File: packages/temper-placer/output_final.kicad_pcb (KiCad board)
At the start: 4 copper layers, 100 x 150 mm, 33 parts, among them Q1 IKW40N120H3, Q2 IKW40N120H3

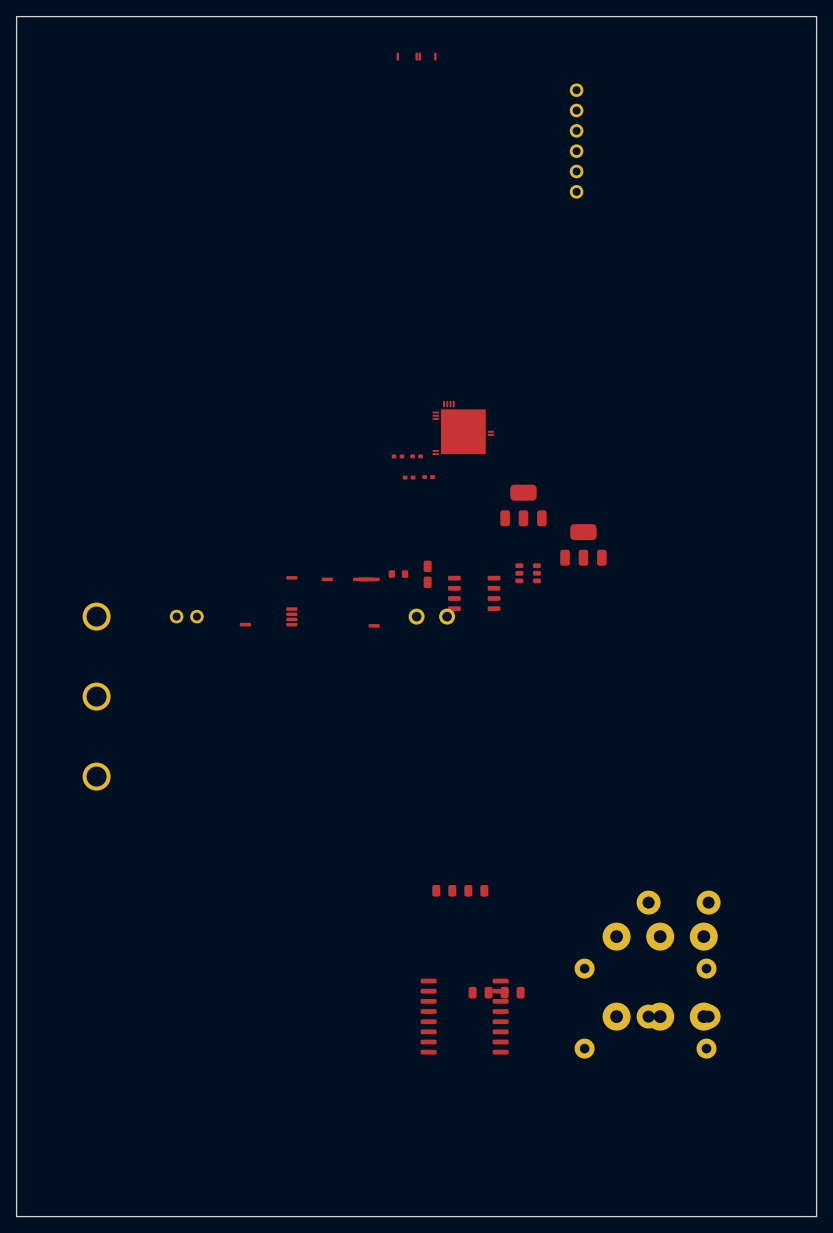
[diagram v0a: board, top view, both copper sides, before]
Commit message: fix: Recalculate fixed positions to prevent overlaps
ROOT CAUSE: The original fixed positions assumed small components,
but actual THT packages are much larger:
- Q1/Q2 (IGBTs): 14.4mm wide
- D1/D2 (Diodes): 17.7mm wide
- C_BUS1/2: 10.5mm wide
- U_GATE: 11.0mm × 9.5mm

Original layout had ~12mm of overlap between adjacent components!

NEW POSITIONS (non-overlapping with 1mm margin):
- Q1: (75, 130), Q2: (75, 118) - 12mm vertical spacing
- D1: (58, 130), D2: (58, 118) - 17mm left of Q
- C_BUS1/2: (89, 130/118) - 14mm right of Q
- U_GATE: (40, 124) - clear of diodes
- C_BOOT/C_VCC: (37/43, 132) - above U_GATE

Verified: No overlaps between any fixed components.
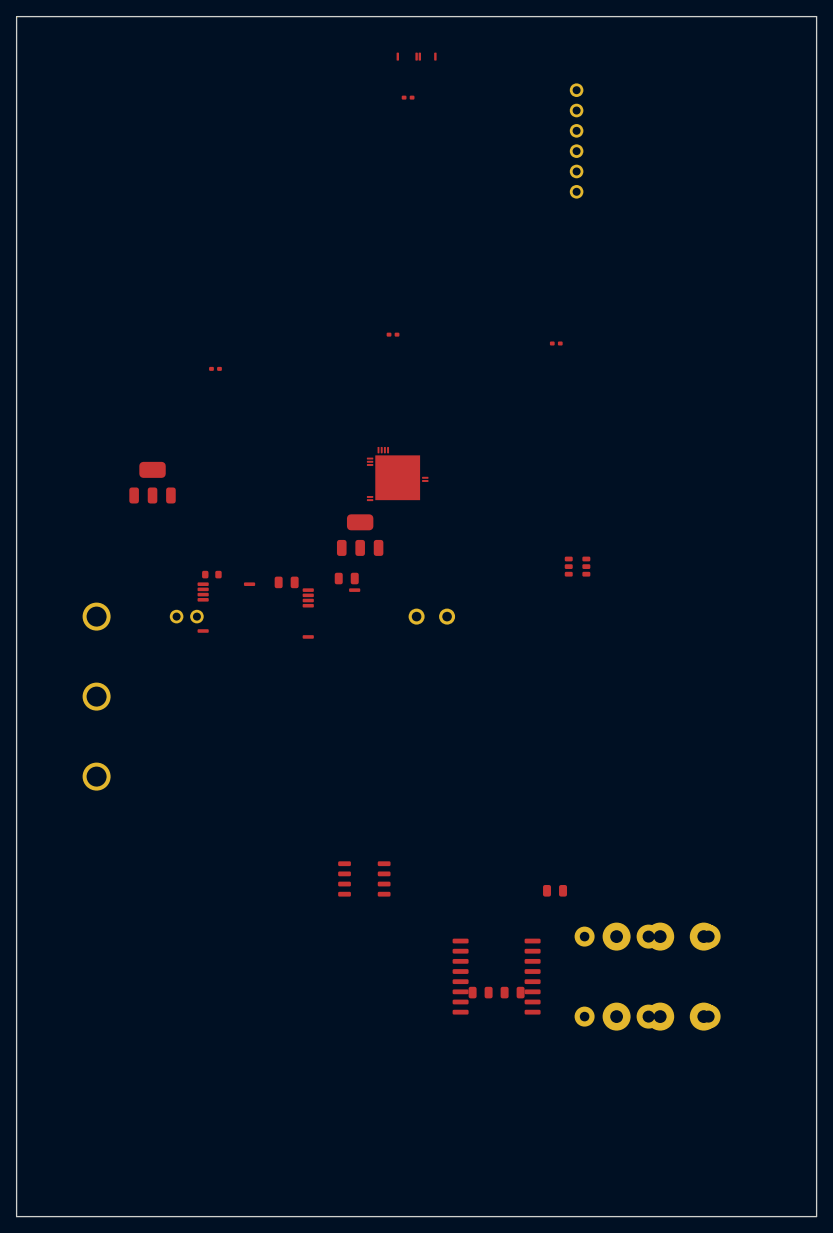
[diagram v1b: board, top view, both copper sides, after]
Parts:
- moved U_LDO_3V3 46.5 mm to (17.0, 59.9)
- moved C_MCU_4 44.9 mm to (48.9, 10.1)
- moved R_GATE_H 42.3 mm to (41.3, 70.2)
- moved U_OPAMP_CT 38.2 mm to (43.5, 107.8)
- moved U_LDO_5V 27.9 mm to (42.9, 66.4)
- moved C_MCU_3 25.3 mm to (24.9, 44.0)
- moved C_CT_FILT 23.3 mm to (24.4, 69.8)
- moved C_MCU_2 23.1 mm to (67.5, 40.9)
- moved C_MCU_1 18.0 mm to (47.1, 39.8)
- moved R_BURDEN 17.7 mm to (33.8, 70.7), turned to 0 degrees
- moved MAX31865 15.6 mm to (26.2, 73.9), turned to 0 degrees
- moved R_GATE_L 13.8 mm to (67.3, 109.3)
- moved U_MCU 10.0 mm to (47.6, 57.6)
- moved U_CT 8.00 mm to (39.4, 74.6), turned to 0 degrees
- moved U_GATE 6.40 mm to (60.0, 120.0)
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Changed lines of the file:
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@@
   )
   (footprint "Diode_THT:D_DO-201AD_P15.24mm_Horizontal" (layer "F.Cu")
-    (at 71.0 129.0 0.0)
+    (at 71.0 125.0 0.0)
     (property "Reference" "D1")
     (property "Value" "1N5408")
@@
   )
   (footprint "Diode_THT:D_DO-201AD_P15.24mm_Horizontal" (layer "F.Cu")
-    (at 71.0 119.0 0.0)
+    (at 71.0 115.0 0.0)
     (property "Reference" "D2")
     (property "Value" "1N5408")
@@
   )
   (footprint "Capacitor_THT:CP_Radial_D18.0mm_P7.50mm" (layer "F.Cu")
-    (at 79.0 110.75 0.0)
+    (at 79.0 115.0 0.0)
     (property "Reference" "C_BUS2")
     (property "Value" "330uF/400V")
@@
   )
   (footprint "Package_SO:SOIC-16W_7.5x10.3mm_P1.27mm" (layer "F.Cu")
-    (at 56.005001068115234 125.0 0.0)
+    (at 60.0 120.0 0.0)
     (property "Reference" "U_GATE")
     (property "Value" "UCC21550")
@@
   )
   (footprint "Resistor_SMD:R_0805_2012Metric" (layer "F.Cu")
-    (at 57.46479034423828 109.2750015258789 0.0)
+    (at 41.26744842529297 70.24166870117188 0.0)
     (property "Reference" "R_GATE_H")
     (property "Value" "4.7R")
@@
   )
   (footprint "Resistor_SMD:R_0805_2012Metric" (layer "F.Cu")
-    (at 53.45823287963867 109.2750015258789 0.0)
+    (at 67.30274963378906 109.2750015258789 0.0)
     (property "Reference" "R_GATE_L")
     (property "Value" "4.7R")
@@
   )
   (footprint "Package_TO_SOT_SMD:SOT-23-6" (layer "F.Cu")
-    (at 63.94453811645508 69.58772277832031 0.0)
+    (at 70.11795806884766 68.75 0.0)
     (property "Reference" "U_BUCK")
     (property "Value" "LMR51430")
@@
   )
   (footprint "Package_TO_SOT_SMD:SOT-223-3_TabPin2" (layer "F.Cu")
-    (at 63.358741760253906 62.70867919921875 0.0)
+    (at 16.99129295349121 59.859886169433594 0.0)
     (property "Reference" "U_LDO_3V3")
     (property "Value" "AMS1117-3.3")
@@
   )
   (footprint "Package_TO_SOT_SMD:SOT-223-3_TabPin2" (layer "F.Cu")
-    (at 70.85382080078125 67.63876342773438 0.0)
+    (at 42.94513702392578 66.41667175292969 0.0)
     (property "Reference" "U_LDO_5V")
     (property "Value" "AMS1117-5.0")
@@
   )
   (footprint "Package_DFN_QFN:QFN-56-1EP_7x7mm_P0.4mm_EP5.6x5.6mm" (layer "F.Cu")
-    (at 55.842281341552734 51.89179992675781 0.0)
+    (at 47.6356086730957 57.64506530761719 0.0)
     (property "Reference" "U_MCU")
     (property "Value" "ESP32-S3-WROOM-1")
@@
   )
   (footprint "Capacitor_SMD:C_0402_1005Metric" (layer "F.Cu")
-    (at 49.06879806518555 57.62437057495117 0.0)
+    (at 47.05330276489258 39.75304412841797 0.0)
     (property "Reference" "C_MCU_1")
     (property "Value" "100nF")
@@
   )
   (footprint "Capacitor_SMD:C_0402_1005Metric" (layer "F.Cu")
-    (at 51.49932861328125 57.554359436035156 0.0)
+    (at 67.46141815185547 40.86226272583008 0.0)
     (property "Reference" "C_MCU_2")
     (property "Value" "100nF")
@@
   )
   (footprint "Capacitor_SMD:C_0402_1005Metric" (layer "F.Cu")
-    (at 47.67693328857422 54.983089447021484 0.0)
+    (at 24.86142349243164 44.03423309326172 0.0)
     (property "Reference" "C_MCU_3")
     (property "Value" "100nF")
@@
   )
   (footprint "Capacitor_SMD:C_0402_1005Metric" (layer "F.Cu")
-    (at 50.002864837646484 54.97755432128906 0.0)
+    (at 48.93632125854492 10.12717342376709 0.0)
     (property "Reference" "C_MCU_4")
     (property "Value" "10uF")
@@
   )
   (footprint "Package_SO:TSSOP-20_4.4x6.5mm_P0.65mm" (layer "F.Cu")
-    (at 31.504030227661133 73.08263397216797 180.0)
+    (at 39.3566780090332 74.61666107177734 0.0)
     (property "Reference" "U_CT")
     (property "Value" "MAX31865")
@@
   )
   (footprint "Resistor_SMD:R_0805_2012Metric" (layer "F.Cu")
-    (at 51.37902069091797 69.716552734375 90.0)
+    (at 33.75667953491211 70.7249984741211 0.0)
     (property "Reference" "R_BURDEN")
     (property "Value" "33R")
@@
   )
   (footprint "Capacitor_SMD:C_0603_1608Metric" (layer "F.Cu")
-    (at 47.7335205078125 69.68580627441406 0.0)
+    (at 24.40990447998047 69.75 0.0)
     (property "Reference" "C_CT_FILT")
     (property "Value" "100pF")
@@
   )
   (footprint "Package_SO:SOIC-8_3.9x4.9mm_P1.27mm" (layer "F.Cu")
-    (at 57.20094299316406 72.10311889648438 0.0)
+    (at 43.46776580810547 107.79499816894531 0.0)
     (property "Reference" "U_OPAMP_CT")
     (property "Value" "LM358")
@@
   )
   (footprint "Package_SO:TSSOP-20_4.4x6.5mm_P0.65mm" (layer "F.Cu")
-    (at 41.77537536621094 73.254150390625 270.0)
+    (at 26.219999313354492 73.875 0.0)
     (property "Reference" "MAX31865")
     (property "Value" "MAX31865")
